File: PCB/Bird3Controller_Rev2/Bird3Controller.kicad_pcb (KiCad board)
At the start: 2 copper layers, 43 x 108 mm, 52 parts, among them IC1 M24C08-RMN6TP, J1 Bird 3 24-pin Connector, J2 TXW154028S0 Connector, J3 87832-2220, Q1 2N7002A, SW1 SW_Boot, SW2 SW_Reset, U1 ESP32-S3-WROOM-1, U3 SN65HVD231, U4 LMR36520ADDAR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

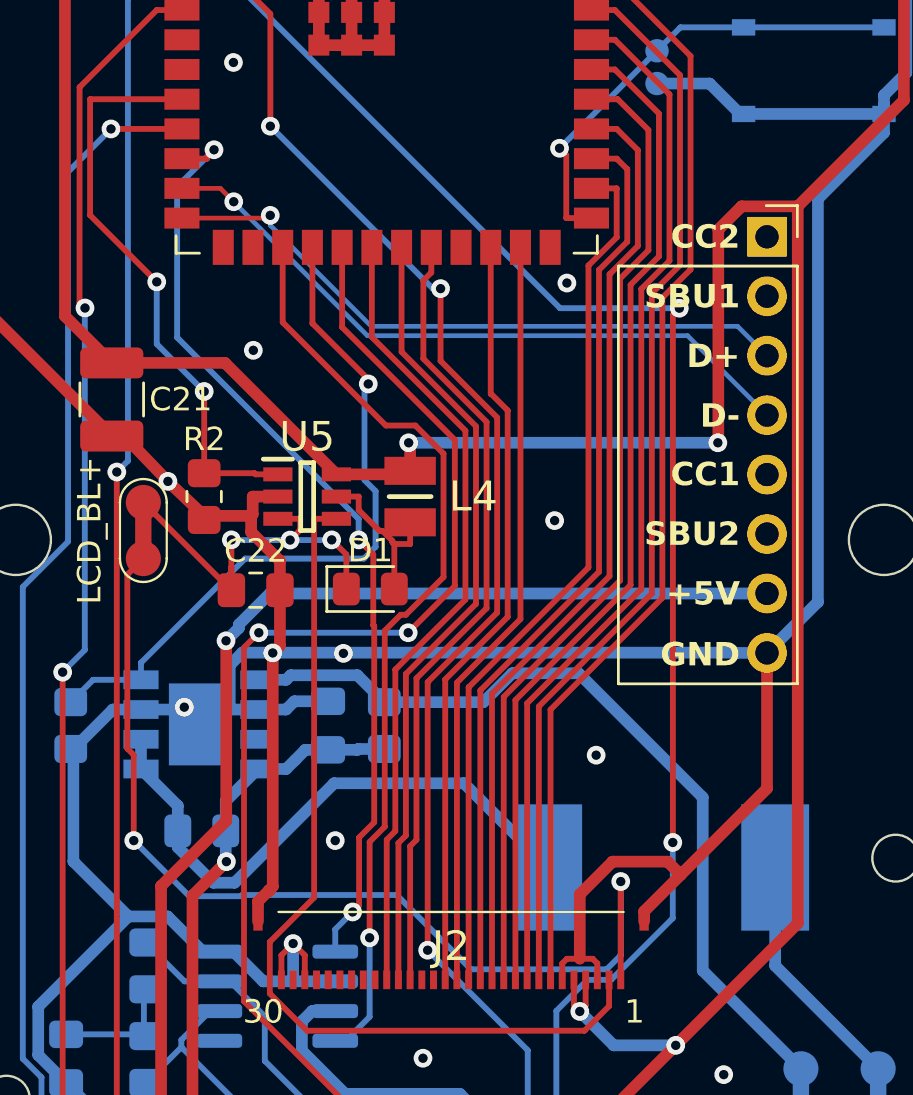
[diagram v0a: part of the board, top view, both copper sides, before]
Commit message: Move things around to eliminate two vias in the CAN_TX trace
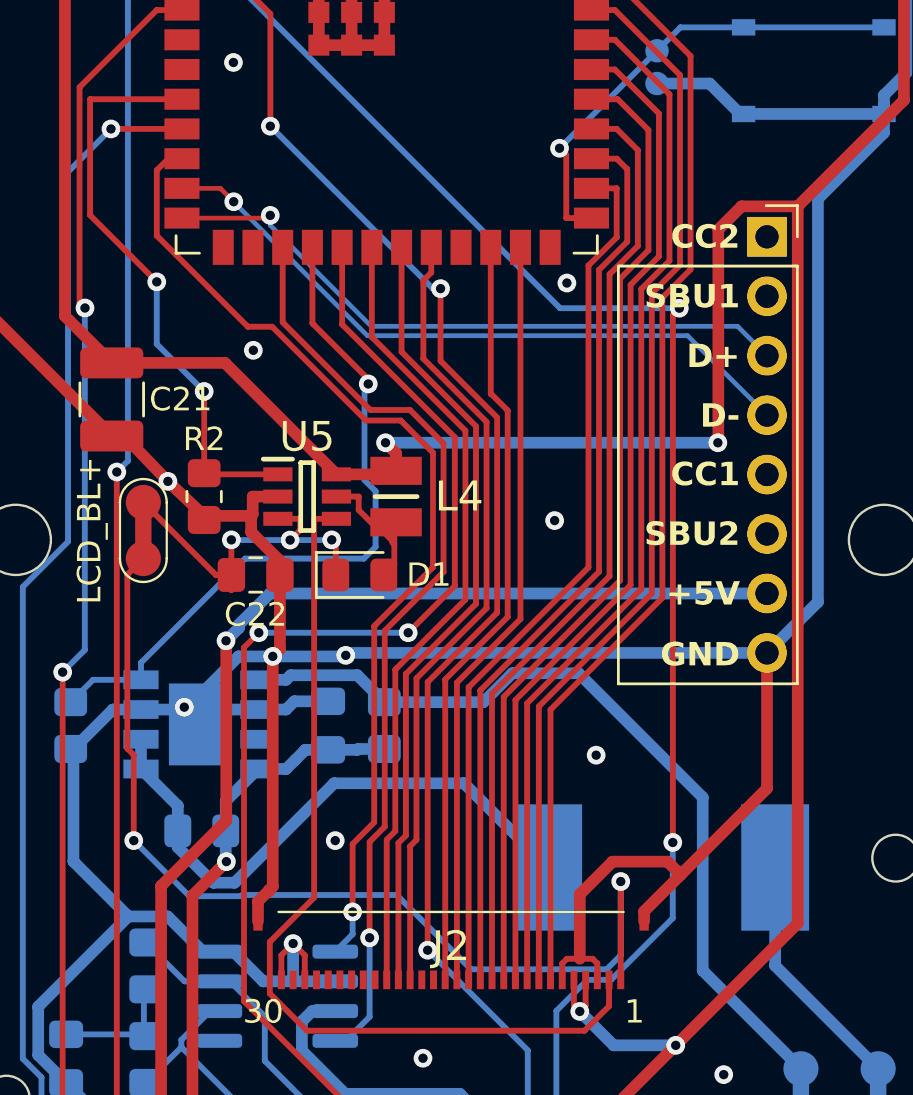
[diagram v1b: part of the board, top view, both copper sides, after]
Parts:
- moved D1 0.75 mm to (178.1, 84.7)
- moved C22 0.65 mm to (173.7, 84.7)
- moved L4 0.60 mm to (179.7, 81.3)
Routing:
- net GND: track 421.4 -> 423.9 mm
- net /CAN_TX: track 40.7 -> 42.8 mm, vias 3 -> 1
- net Net-(D1-K): track 17.8 -> 16.1 mm
- net Net-(D1-A): track 7.21 -> 6.16 mm

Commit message: Push more things around
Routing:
- net /CAN_L: track 29.3 -> 31.2 mm
- net /THR1: track 83.6 -> 84.7 mm
- net /LED_SIG: track 30.3 -> 29.3 mm
- net /CAN_H: track 28.2 -> 27.4 mm
- net /BR2: track 91.4 -> 90.7 mm
- net GND: track 423.9 -> 424.6 mm, vias 18 -> 19

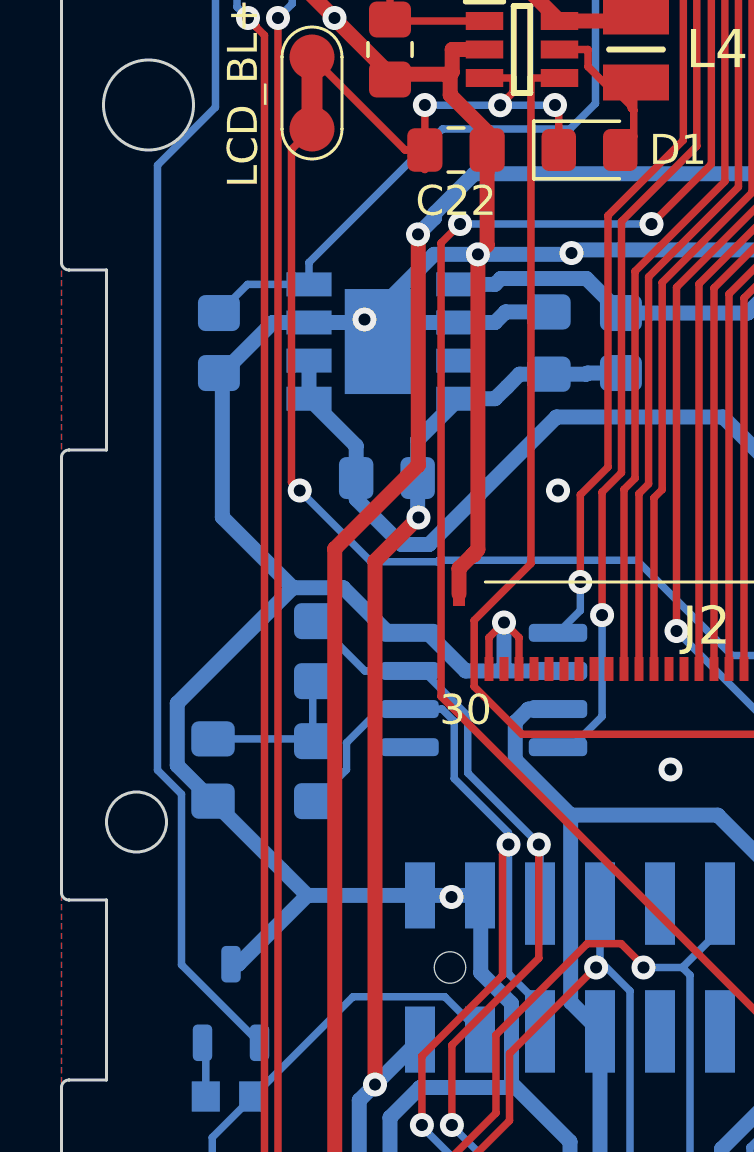
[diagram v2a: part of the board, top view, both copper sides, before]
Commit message: Move vias around a bit
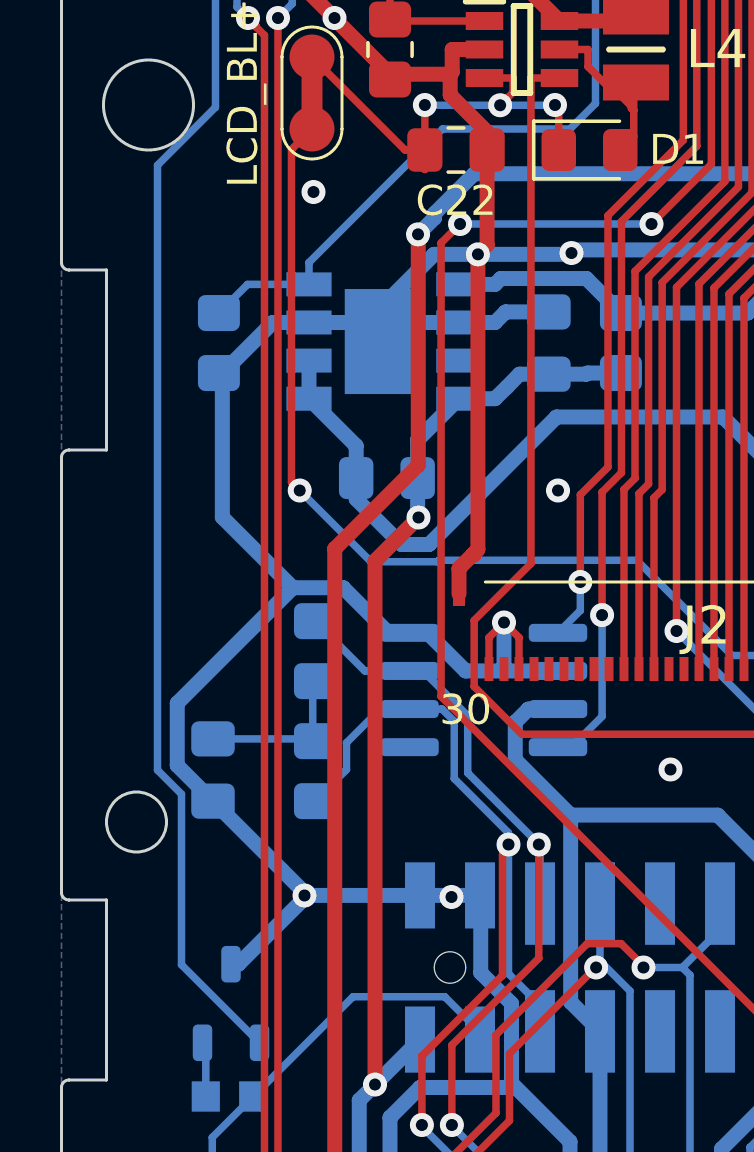
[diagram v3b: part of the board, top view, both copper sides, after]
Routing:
- net GND: vias 19 -> 20
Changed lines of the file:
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@@
-	)
-	(via
-		(at 170.6 90.35)
-		(size 0.8)
-		(drill 0.4)
-		(layers "F.Cu" "B.Cu")
-		(net 5)
 	)
 	(via
@@
 	)
 	(via
+		(at 168.6 109.55)
+		(size 0.8)
+		(drill 0.4)
+		(layers "F.Cu" "B.Cu")
+		(net 5)
+	)
+	(via
 		(at 173.5 109.6)
 		(size 0.8)
@@
 	(via
 		(at 169.7 126.35)
+		(size 0.8)
+		(drill 0.4)
+		(layers "F.Cu" "B.Cu")
+		(free yes)
+		(net 5)
+	)
+	(via
+		(at 168.9 86.1)
 		(size 0.8)
 		(drill 0.4)
@@
 	)
 	(segment
+		(start 168.69 109.55)
+		(end 168.6 109.55)
+		(width 0.5)
+		(layer "B.Cu")
+		(net 5)
+	)
+	(segment
 		(start 180.91 142.262)
 		(end 180.91 141.655)
@@
 	)
 	(segment
+		(start 168.6 109.55)
+		(end 168.6 109.64)
+		(width 0.5)
+		(layer "B.Cu")
+		(net 5)
+	)
+	(segment
 		(start 165.861 92.135)
 		(end 165.748 92.135)
@@
 	)
 	(segment
+		(start 168.6 109.64)
+		(end 166.4 111.84)
+		(width 0.5)
+		(layer "B.Cu")
+		(net 5)
+	)
+	(segment
 		(start 173.4475 109.5475)
 		(end 168.6925 109.5475)
@@
 	(segment
 		(start 168.6925 109.5475)
-		(end 166.4 111.84)
-		(width 0.5)
-		(layer "B.Cu")
+		(end 168.69 109.55)
+		(width 0.5)
+		(layer "B.Cu")
